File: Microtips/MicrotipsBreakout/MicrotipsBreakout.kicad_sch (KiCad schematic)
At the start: 16 parts, among them J1 Conn_01x24_Pin, Q1 Si1308EDL

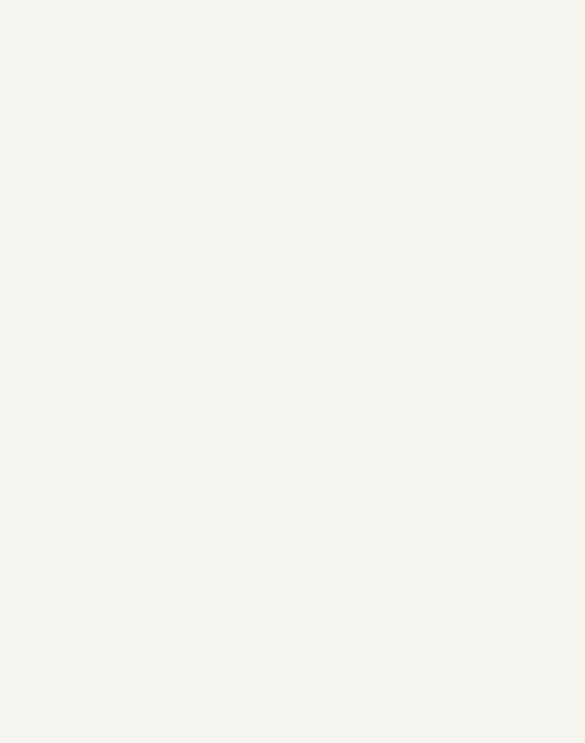
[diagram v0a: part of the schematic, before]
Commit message: Added Pico
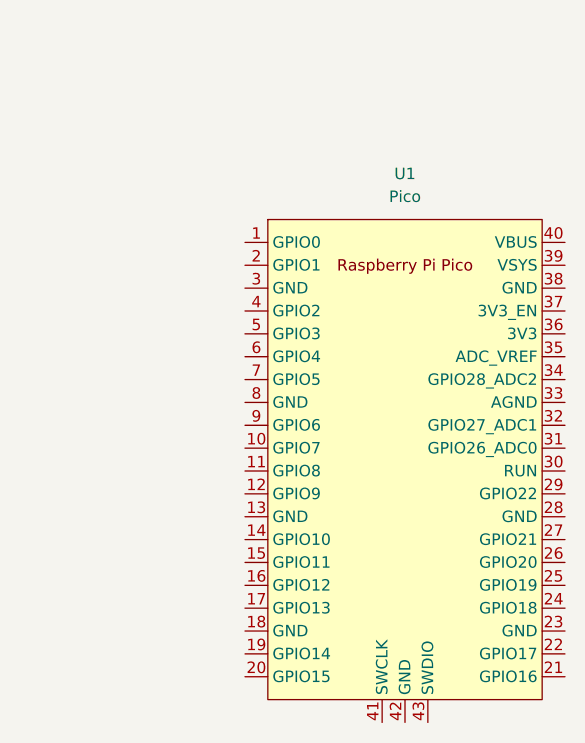
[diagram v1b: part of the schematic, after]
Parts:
- added U1: Pico, MCU_RaspberryPi_and_Boards:RPi_Pico_SMD_TH, symbol PicoW:Pico
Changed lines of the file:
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@@
+	)
+	(symbol
+		(lib_id "PicoW:Pico")
+		(at 240.03 73.66 0)
+		(unit 1)
+		(exclude_from_sim no)
+		(in_bom yes)
+		(on_board yes)
+		(dnp no)
+		(fields_autoplaced yes)
+		(property "Reference" "U1"
+			(at 240.03 41.91 0)
+			(effects
+				(font
+					(size 1.27 1.27)
+				)
+			)
+		)
+		(property "Value" "Pico"
+			(at 240.03 44.45 0)
+			(effects
+				(font
+					(size 1.27 1.27)
+				)
+			)
+		)
+		(property "Footprint" "MCU_RaspberryPi_and_Boards:RPi_Pico_SMD_TH"
+			(at 240.03 73.66 90)
+			(effects
+				(font
+					(size 1.27 1.27)
+				)
+				(hide yes)
+			)
+		)
+		(property "Datasheet" ""
+			(at 240.03 73.66 0)
+			(effects
+				(font
+					(size 1.27 1.27)
+				)
+				(hide yes)
+			)
+		)
+		(property "Description" ""
+			(at 240.03 73.66 0)
+			(effects
+				(font
+					(size 1.27 1.27)
+				)
+				(hide yes)
+			)
+		)
+		(pin "22"
+		)
+		(pin "7"
+		)
+		(pin "30"
+		)
+		(pin "6"
+		)
+		(pin "18"
+		)
+		(pin "15"
+		)
+		(pin "14"
+		)
+		(pin "25"
+		)
+		(pin "35"
+		)
+		(pin "23"
+		)
+		(pin "2"
+		)
+		(pin "4"
+		)
+		(pin "16"
+		)
+		(pin "26"
+		)
+		(pin "34"
+		)
+		(pin "39"
+		)
+		(pin "43"
+		)
+		(pin "21"
+		)
+		(pin "1"
+		)
+		(pin "8"
+		)
+		(pin "37"
+		)
+		(pin "17"
+		)
+		(pin "10"
+		)
+		(pin "27"
+		)
+		(pin "29"
+		)
+		(pin "31"
+		)
+		(pin "40"
+		)
+		(pin "9"
+		)
+		(pin "28"
+		)
+		(pin "11"
+		)
+		(pin "33"
+		)
+		(pin "38"
+		)
+		(pin "32"
+		)
+		(pin "41"
+		)
+		(pin "3"
+		)
+		(pin "12"
+		)
+		(pin "5"
+		)
+		(pin "20"
+		)
+		(pin "36"
+		)
+		(pin "19"
+		)
+		(pin "24"
+		)
+		(pin "13"
+		)
+		(pin "42"
+		)
+		(instances
+			(project ""
+				(path "/55ca8b29-25a3-4dc3-aa16-05bc347fe3c5"
+					(reference "U1")
+					(unit 1)
+				)
+			)
+		)
 	)
 	(symbol

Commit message: made graphics; building EPD driver
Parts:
- added C10, C11, C12, C13, C16, C17: 10uF, Capacitor_Tantalum_SMD:CP_EIA-3528-12_Kemet-T, symbol Device:C_Polarized_US
- added C14, C15: 10uF, Capacitor_SMD:C_1206_3216Metric, symbol Device:C_Polarized_US
- added J3: Conn_01x02_Socket, Connector_PinSocket_2.54mm:PinSocket_1x02_P2.54mm_Vertical, symbol Connector:Conn_01x02_Socket
- added L2: L, Inductor_SMD:L_Chilisin_BMRB00050518-B, symbol Device:L
- added P1, P2, P3, P4: ~, WuerthMounting:9774060360R, symbol WurthMounting:9774060360R
- added Q2, Q5: PNP, Package_TO_SOT_SMD:SOT-23, symbol Simulation_SPICE:PNP
- added Q3, Q4: PMOS, Package_TO_SOT_SMD:SOT-23, symbol Simulation_SPICE:PMOS
- added R2, R3: 5.1k, Resistor_SMD:R_0603_1608Metric, symbol Device:R
- added R4, R5, R6: 100k, Resistor_SMD:R_0603_1608Metric, symbol Device:R
- added R7: 61.9k, Resistor_SMD:R_0603_1608Metric, symbol Device:R
- added R8: 20k, Resistor_SMD:R_0603_1608Metric, symbol Device:R
- added U2: TYPE-C 16PLT-H10.0, EasyEDA:TYPE-C-SMD_USB4120-03-C, symbol EasyEDA:TYPE-C16PLT-H10.0
- added U3: TPS560200, Package_TO_SOT_SMD:SOT-23-5, symbol Regulator_Switching:TPS560200
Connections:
- net TSDA is gone; now on an unnamed net: J1.7 (Pin_7)
- net BS: now also J1.17 (Pin_17), U1.31 (GPIO26_ADC0); no longer J1.8 (Pin_8)
- net BUSY: now also J1.16 (Pin_16), U1.29 (GPIO22); no longer J1.9 (Pin_9)
- net CS#: now also J1.13 (Pin_13), U1.22 (GPIO17); no longer J1.12 (Pin_12)
- net D/C#: now also J1.14 (Pin_14), U1.26 (GPIO20); no longer J1.11 (Pin_11)
- net GDR: now also J1.23 (Pin_23); no longer J1.2 (Pin_2)
- net GND: now also J1.18 (Pin_18), J1.19 (Pin_19), J1.8 (Pin_8), U1.13 (GND), U1.18 (GND), U1.23 (GND), U1.28 (GND), U1.3 (GND), U1.38 (GND), U1.42 (GND), U1.8 (GND), C10.2, C11.2, C12.2, C13.2, C14.2, C15.2, C16.2, C17.2, J3.1 (Pin_1), R2.2, R3.1, R4.2, R5.2, R6.2, R8.2, U2.0 (EH), U2.A1 (GND), U2.A12 (GND), U2.B1 (GND), U2.B12 (GND), U3.2 (GND); no longer J1.17 (Pin_17)
- net RES#: now also J1.15 (Pin_15), U1.27 (GPIO21); no longer J1.10 (Pin_10)
- net RESE: now also J1.22 (Pin_22); no longer J1.3 (Pin_3)
- net SCL: now also J1.12 (Pin_12), U1.24 (GPIO18); no longer J1.13 (Pin_13)
- net SDA: now also J1.11 (Pin_11), U1.25 (GPIO19); no longer J1.14 (Pin_14)
- net VGH: now also J1.4 (Pin_4); no longer J1.21 (Pin_21)
- net VGL: now also J1.2 (Pin_2); no longer J1.23 (Pin_23)
- net at C7.1: now also J1.5 (Pin_5); no longer J1.20 (Pin_20)
- net at C6.1: no longer J1.18 (Pin_18)
- net at C9.1: now also J1.1 (Pin_1); no longer J1.24 (Pin_24)
- net at C5.1: now also J1.20 (Pin_20); no longer J1.5 (Pin_5)
- net at C8.1: now also J1.3 (Pin_3); no longer J1.22 (Pin_22)
- net +3V3: now reaches U1.39 (VSYS)
- net +3V3: now also C4.1, J1.10 (Pin_10), J1.9 (Pin_9), L1.1, C15.1, C16.1, C17.1, L2.2, R7.1
- net TSCL: no longer names the net of J1.6 (Pin_6)
- removed net VCI: C4.1, J1.15 (Pin_15), J1.16 (Pin_16), L1.1
- new net: R2.1, U2.B5 (CC2)
- new net: Q2.1 (B), Q5.1 (B), R5.1
- new net: Q2.3 (C), Q4.1 (G), R4.1
- new net: Q3.1 (G), Q5.3 (C), R6.1
- new net: R3.2, U2.A5 (CC1)
- new net: R7.2, R8.1, U3.5 (FB)
- new net: L2.1, U3.3 (PH)
- new net +12V: C12.1, C13.1, J3.2 (Pin_2), Q4.3 (D)
- new net USB_DN: U2.A7 (DN1), U2.B7 (DN2)
- new net USB_DP: U2.A6 (DP1), U2.B6 (DP2)
- new net VIN: C14.1, Q3.2 (S), Q4.2 (S), Q5.2 (E), U3.4 (VIN)
- new net V_USB: C10.1, C11.1, Q2.2 (E), Q3.3 (D), U2.A4 (VBUS), U2.A9 (VBUS), U2.B4 (VBUS), U2.B9 (VBUS)
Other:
- note added: "10"
- note added: "11"
- note added: "12"
- note added: "13"
- note added: "14"
- note added: "15"
- note added: "16"
- note added: "17"
- note added: "18"
- note added: "19"
- note added: "20"
- note added: "21"
- note added: "22"
- note added: "23"
- note added: "24"
- note added: "5"
- note added: "6"
- note added: "7"
- note added: "8"
- note added: "9"
- moved on the sheet: J1, U1
